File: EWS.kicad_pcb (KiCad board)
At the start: 4 copper layers, 65 x 56 mm, 121 parts, among them J301 GPIO, J401 XT30, J402 MX3.0 2x2, J403 MX3.0 2x2, J404 USB-C, J405 USB-C, J406 USB-A, Q401 CJAC70P06, Q402 CJAC70P06, Q403 AO3400A, Q404 AO3400A, SW301 TS-1088, SW302 TS-1088, U201 XC6206P332MR, U202 XR76208, U301 TJA1051TK-3, U302 STM32G0B1KBUx, U401 CH334F, U402 USBLC6-2SC6, U403 USBLC6-2SC6, U404 USBLC6-2SC6

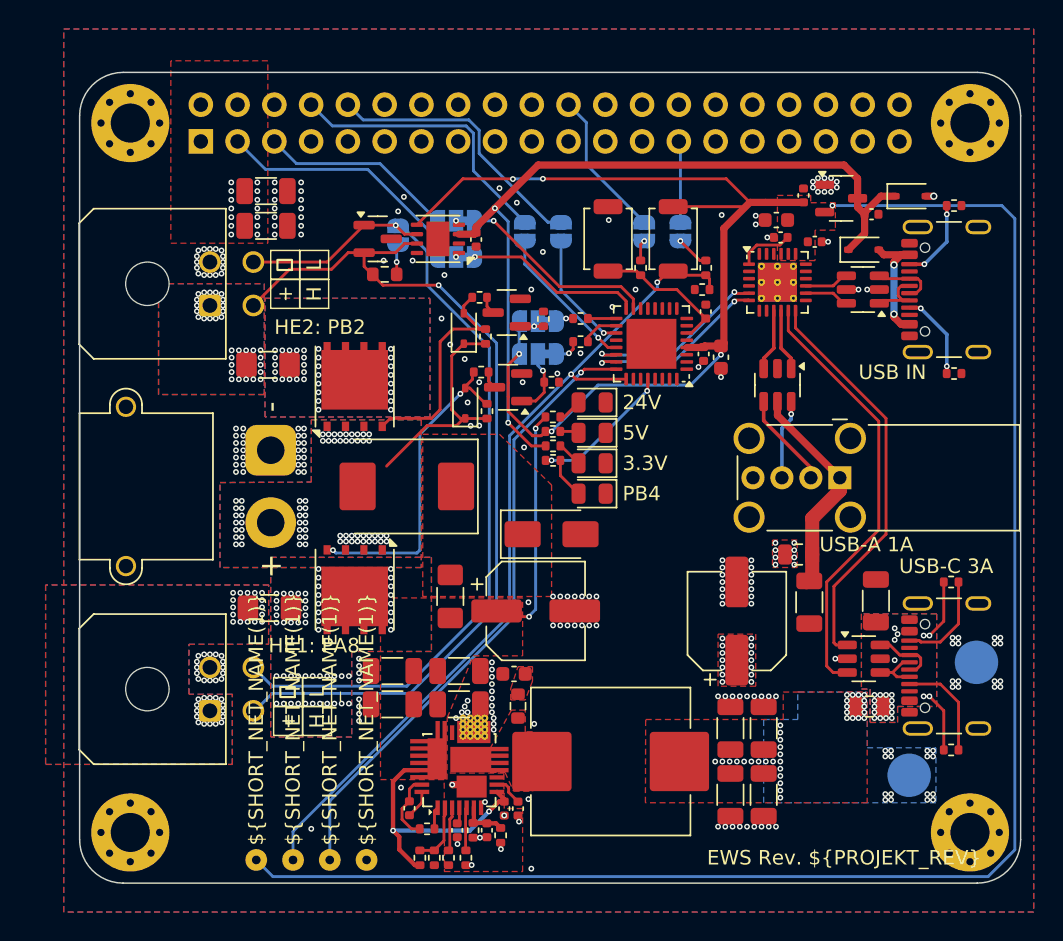
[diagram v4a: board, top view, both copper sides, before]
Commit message: Rev. 0.3: Add 10µF capacitor C304 to CAN transceiver and QR code placeholder
- Added 10µF capacitor C304 for improved CAN communication stability
- Added QR code placeholder for serial number on PCB
- Enhanced signal integrity with additional filtering at CAN transceiver
- Improved traceability with unique identification capability
- Updated changelogs and documentation for Rev. 0.3
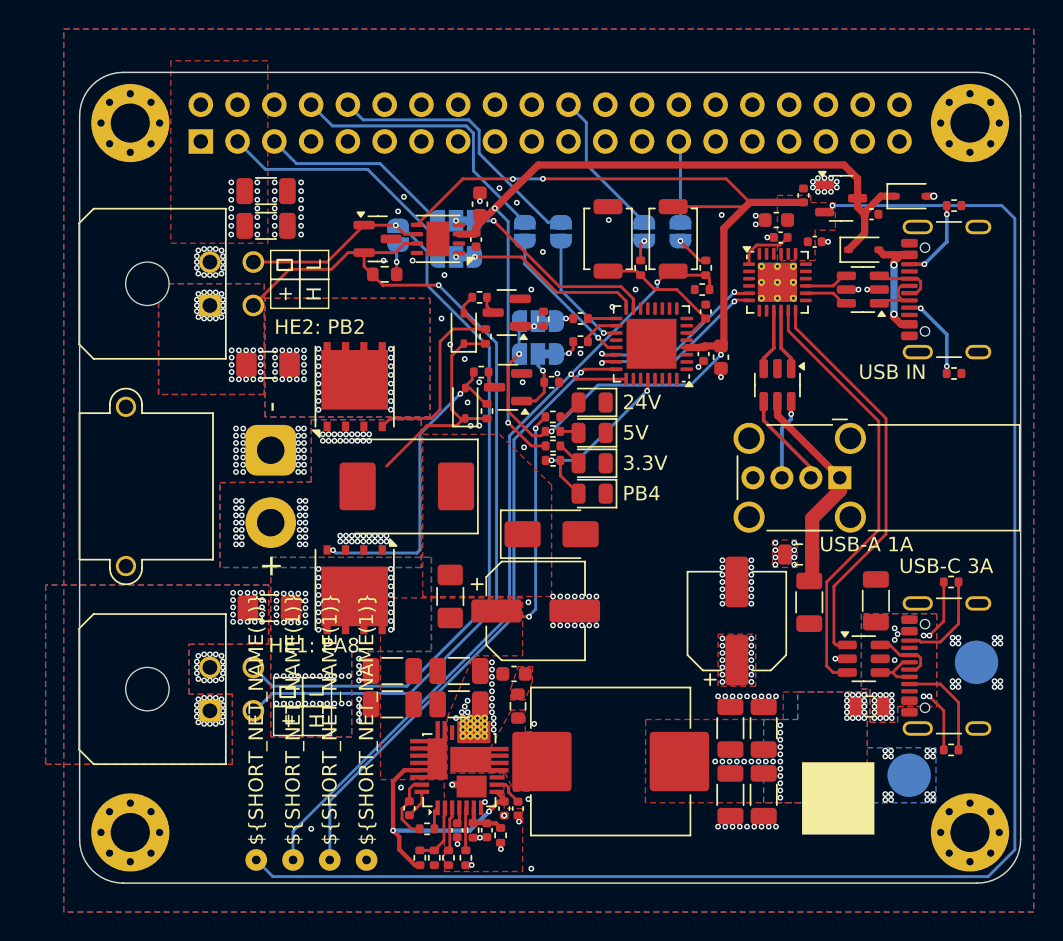
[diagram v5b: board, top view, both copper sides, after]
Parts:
- added C304: 10u, Capacitor_SMD:C_0603_1608Metric, F.Cu at (157.7, 76.1)
- renumbered C304 to C305, C305 to C306, C306 to C307
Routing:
- net GND: vias 210 -> 211
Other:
- board text removed: "EWS Rev. ${PROJEKT_REV}"

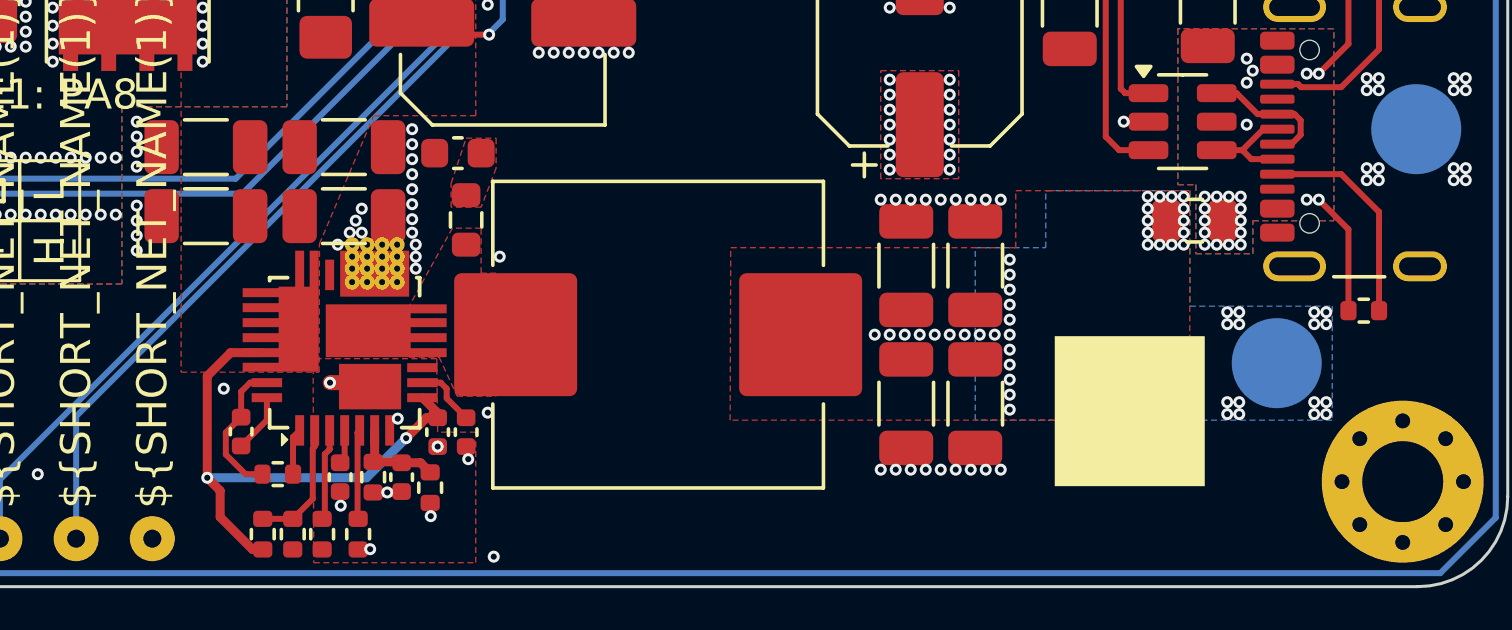
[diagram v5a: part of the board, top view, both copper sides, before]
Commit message: Production Optimization: JLCPCB assembly improvements
- Excluded test points TP202/TP203 from BOM
- Set FT rotation offsets for automated assembly:
  - U202/U301: 270° rotation offset
  - U401: 180° rotation offset
- Updated production data for JLCPCB compatibility
- Added unreleased changelog section for tracking
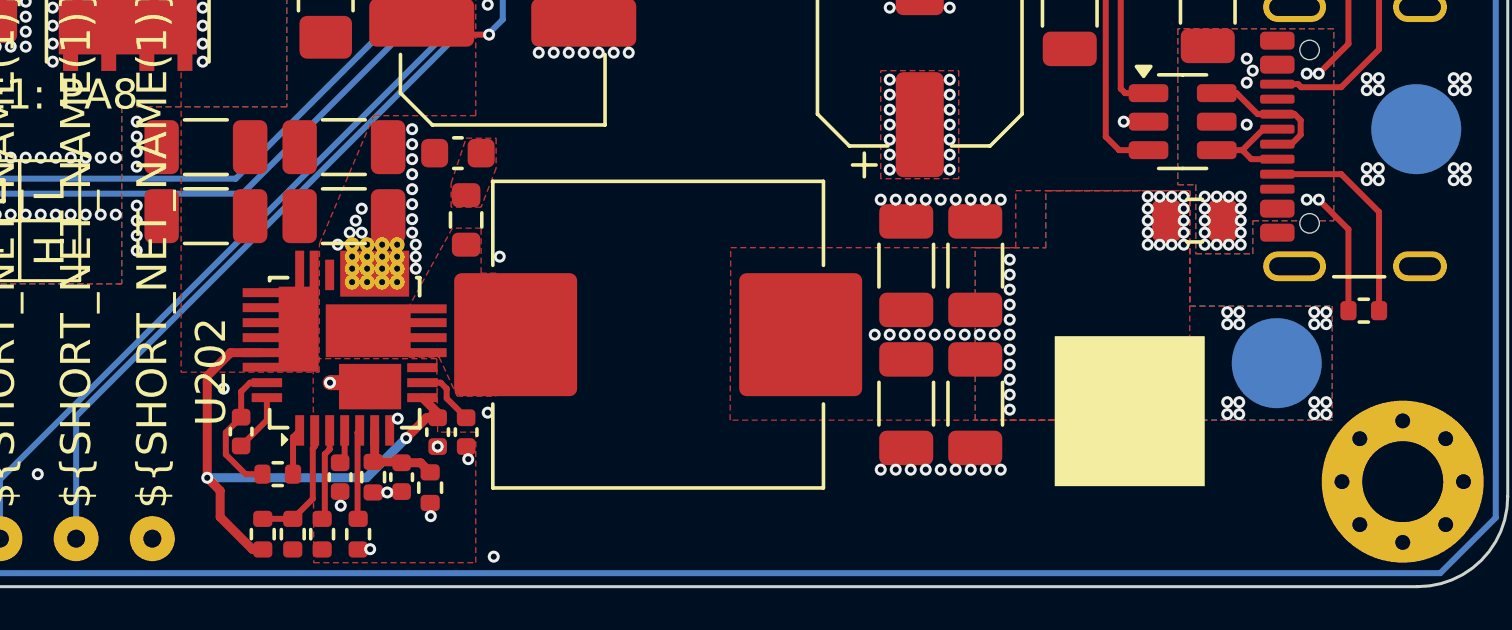
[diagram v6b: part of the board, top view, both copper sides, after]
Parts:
- U202: footprint project:IC_XR76203ELTR-F -> project:IC_XR76208ELTR-F
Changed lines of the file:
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@@
 			)
 		)
+		(property "FT Rotation Offset" "270"
+			(at 0 0 180)
+			(unlocked yes)
+			(layer "F.Fab")
+			(hide yes)
+			(effects
+				(font
+					(size 1 1)
+					(thickness 0.15)
+				)
+			)
+		)
 		(property ki_fp_filters "*VSON*3x3mm*P0.65mm*EP1.6*x2.4*")
 		(sheetname "/MCU/")
@@
 		)
 	)
-	(footprint "project:IC_XR76203ELTR-F"
+	(footprint "project:IC_XR76208ELTR-F"
 		(layer "F.Cu")
 		(at 156.23 115.2 90)
 		(property "Reference" "U202"
-			(at -0.6175 -6.0325 90)
+			(at -0.63595 -4.45165 90)
 			(layer "F.SilkS")
-			(hide yes)
 			(effects
 				(font
@@
 			(at 6.36171 4.45318 90)
 			(layer "F.Fab")
-			(hide yes)
 			(effects
 				(font
@@
 			)
 		)
+		(property "FT Rotation Offset" "270"
+			(at 0 0 90)
+			(unlocked yes)
+			(layer "F.Fab")
+			(hide yes)
+			(effects
+				(font
+					(size 1 1)
+					(thickness 0.15)
+				)
+			)
+		)
 		(sheetname "/Power/")
 		(sheetfile "power.kicad_sch")
@@
 		(sheetname "/Power/")
 		(sheetfile "power.kicad_sch")
-		(attr exclude_from_pos_files)
+		(attr exclude_from_pos_files exclude_from_bom)
 		(fp_circle
 			(center 0 0)
@@
 		(sheetname "/Power/")
 		(sheetfile "power.kicad_sch")
-		(attr exclude_from_pos_files)
+		(attr exclude_from_pos_files exclude_from_bom)
 		(fp_circle
 			(center 0 0)
@@
 	)
 	(zone
+		(net 8)
+		(net_name "5V")
+		(layers "F.Cu" "B.Cu")
+		(hatch edge 0.5)
+		(priority 19)
+		(connect_pads yes
+			(clearance 0.1)
+		)
+		(min_thickness 0.25)
+		(filled_areas_thickness no)
+		(fill yes
+			(thermal_gap 0.5)
+			(thermal_bridge_width 0.5)
+		)
+		(polygon
+			(pts
+				(xy 177.25 111.7) (xy 179.6 111.7) (xy 179.6 109.8) (xy 184.4 109.8) (xy 184.4 113.65) (xy 189.15 113.65)
+				(xy 189.15 117.45) (xy 177.25 117.45)
+			)
+		)
+	)
+	(zone
 		(net 122)
 		(net_name "/Connectivity/OUT1F")
@@
 			)
 		)
-	)
-	(zone
-		(net 8)
-		(net_name "5V")
-		(layer "B.Cu")
-		(hatch edge 0.5)
-		(priority 19)
-		(connect_pads yes
-			(clearance 0.1)
-		)
-		(min_thickness 0.25)
-		(filled_areas_thickness no)
-		(fill yes
-			(thermal_gap 0.5)
-			(thermal_bridge_width 0.5)
-		)
-		(polygon
-			(pts
-				(xy 177.25 111.7) (xy 179.6 111.7) (xy 179.6 109.8) (xy 184.4 109.8) (xy 184.4 113.65) (xy 189.15 113.65)
-				(xy 189.15 117.45) (xy 177.25 117.45)
-			)
-		)
